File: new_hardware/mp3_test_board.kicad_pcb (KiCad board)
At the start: 2 copper layers, 110 x 56 mm, 126 parts, among them J1 PJ-322, J3 TF01-A, P1 TYPE-C 16PIN 2MD(073), P2 WF24LTYAJDNN0#, SW1 K2-1156SP-F5SW-05, SW2 K2-1156SP-F5SW-05, SW3 K2-1156SP-F5SW-05, SW4 K2-1156SP-F5SW-05, SW5 K2-1156SP-F5SW-05, SW6 K2-1156SP-F5SW-05, SW7 GT-TC054A-H035-L1, SW8 GT-TC054A-H035-L1, U1 PCM1795, U14 OPA1656, U15 OPA1656, U2 F133, U3 SGM6603-ADJYN6G, U4 SGM6603-ADJYN6G, U5 SGM3204, U6 LM4562, U7 LM4562, U8 USBLC6-2SC6, U9 MX25L25645GM2I-08G, Y1 12.88727

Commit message: some changes
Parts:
- added D3: PESD3V3L1BA, rlib_passive:D_SOD-323F, F.Cu at (137.2, 96.5)
- added R1: 4.7k, rlib_passive:R_0603_1608Metric, F.Cu at (121.9, 38.1)
- added R14: 10k, rlib_passive:R_0603_1608Metric, F.Cu at (125.9, 38.1)
- added R2: 4.7k, rlib_passive:R_0603_1608Metric, F.Cu at (125.9, 40.6)
- added R4: 1k, rlib_passive:R_0603_1608Metric, F.Cu at (121.9, 40.6)
- added R48: 10k, rlib_passive:R_0603_1608Metric, F.Cu at (96.2, 43.1)
- added R49: 220, rlib_passive:R_0603_1608Metric, F.Cu at (104.2, 43.1)
- added R5: R, rlib_passive:R_0603_1608Metric, F.Cu at (129.9, 38.1)
- added R50: 10k, rlib_passive:R_0603_1608Metric, F.Cu at (100.2, 40.6)
- added R51: 820, rlib_passive:R_0603_1608Metric, F.Cu at (100.2, 48.1)
- added R52: 820, rlib_passive:R_0603_1608Metric, F.Cu at (96.2, 45.6)
- added R53: 820, rlib_passive:R_0603_1608Metric, F.Cu at (96.2, 40.6)
- added R54: 820, rlib_passive:R_0603_1608Metric, F.Cu at (100.2, 43.1)
- added R55: 220, rlib_passive:R_0603_1608Metric, F.Cu at (104.2, 40.6)
- added R56: 220, rlib_passive:R_0603_1608Metric, F.Cu at (112.3, 38.1)
- added R57: 220, rlib_passive:R_0603_1608Metric, F.Cu at (96.2, 38.1)
- added R58: 200, rlib_passive:R_0603_1608Metric, F.Cu at (96.2, 48.1)
- added R59: 200, rlib_passive:R_0603_1608Metric, F.Cu at (108.3, 40.6)
- added R6: R, rlib_passive:R_0603_1608Metric, F.Cu at (129.9, 40.6)
- added R60: 200, rlib_passive:R_0603_1608Metric, F.Cu at (100.2, 45.6)
- added R61: 200, rlib_passive:R_0603_1608Metric, F.Cu at (104.2, 45.6)
- added R62: 180, rlib_passive:R_0603_1608Metric, F.Cu at (104.2, 38.1)
- added R63: 180, rlib_passive:R_0603_1608Metric, F.Cu at (100.2, 38.1)
- added R64: 180, rlib_passive:R_0603_1608Metric, F.Cu at (112.3, 40.6)
- added R65: 180, rlib_passive:R_0603_1608Metric, F.Cu at (108.3, 38.1)
- added R66: 50, rlib_passive:R_0603_1608Metric, F.Cu at (108.3, 43.1)
- added R67: 50, rlib_passive:R_0603_1608Metric, F.Cu at (104.2, 48.1)
- L1, L2: value 4.7u -> 1u
- P1: value TYPE-C 16PIN 2MD(073) -> USB-TYPE-C-018
- R38: value 100 -> 5.1
- moved P1 13.6 mm to (181.0, 99.3)
- moved J1 6.60 mm to (186.8, 72.3)
- moved SW2 4.06 mm to (162.1, 72.2)
- moved SW3 3.83 mm to (162.3, 86.7)
- moved U1 3.59 mm to (162.6, 99.1), turned to 0 degrees
- moved SW6 3.33 mm to (162.8, 101.4)
- moved P2 2.78 mm to (147.7, 108.0)
- moved U2 2.54 mm to (96.5, 86.4)
- moved SW4 2.23 mm to (173.1, 86.9)
- moved SW5 1.19 mm to (153.8, 86.7)
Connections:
- C35 pad 2: Net-(U2-Pad23) -> Net-(C35-Pad2)
- P2 pad 30: Net-(P2-Pad30) -> /SOC/LCD_EN
- R11 pad 1: Net-(P2-Pad30) -> /SOC/LCD_EN
- U2 pad 23: Net-(U2-Pad23) -> Net-(C35-Pad2)
- U2 pad 4: unconnected-(U2-Pad4) -> /SOC/LCD_EN
- U2 pad 53: /NewDAC/I2C_SCL -> /SOC/LCD_CS
- U2 pad 54: /NewDAC/I2C_SDIN -> /SOC/LCD_RD
- U2 pad 75: unconnected-(U2-Pad75) -> /SOC/LCD_WR
- U2 pad 76: unconnected-(U2-Pad76) -> /SOC/LCD_RS
- Y1 pad 1: Net-(U2-Pad23) -> Net-(C35-Pad2)
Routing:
- net /SOC/LCD_D5: track 0.00 -> 16.8 mm
- net GND: track 0.00 -> 0.81 mm

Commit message: xxxx
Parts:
- removed C104, C105, C108, C109, C80, C81, C84, C85, C86, C87, C88, C89, C90, C91: 10u, rlib_passive:T491A106K010AT
- removed C106, C107, C110, C111, C82, C83, C92, C93: 0.1u, rlib_passive:C_0603_1608Metric
- removed the D1 at (63.0, 51.8)
- removed the D1 at (86.4, 129.5)
- removed J3: TF01-A, rlib_connectors:TF-01A
- removed L9: L, rlib_passive:INDC2520X120N
- removed R51, R52, R53, R54: 820, rlib_passive:R_0603_1608Metric
- removed R55, R56, R57: 220, rlib_passive:R_0603_1608Metric
- removed R58, R59, R60, R61: 200, rlib_passive:R_0603_1608Metric
- removed R62, R63, R64, R65: 180, rlib_passive:R_0603_1608Metric
- removed R66, R67: 50, rlib_passive:R_0603_1608Metric
- removed U14, U15: OPA1656, rlib_ic:SOIC-8_3.9x4.9mm_P1.27mm
- removed the U4 at (94.2, 128.7)
- removed the U4 at (66.0, 121.9)
- removed the U5 at (12.7, 9.97)
- removed the U5 at (83.6, 135.8)
- added C1: 100n, rlib_passive:C_0603_1608Metric, F.Cu at (177.3, 118.3)
- added C16: 100n, rlib_passive:C_0603_1608Metric, B.Cu at (82.3, 61.1)
- added C2: 100n, rlib_passive:C_0603_1608Metric, F.Cu at (185.3, 116.6)
- added C3: 100n, rlib_passive:C_0603_1608Metric, B.Cu at (100.2, 63.3)
- added C37: 10u, rlib_passive:T491A106K010AT, B.Cu at (142.1, 73.1)
- added C38: 10u, rlib_passive:T491A106K010AT, B.Cu at (142.0, 67.5)
- added C39: 10u, rlib_passive:T491A106K010AT, B.Cu at (229.1, 125.3)
- added C4: 10u, rlib_passive:C_0603_1608Metric, B.Cu at (101.6, 64.7)
- added C40: 10u, rlib_passive:T491A106K010AT, B.Cu at (224.4, 125.3)
- added C41: 2.2n, rlib_passive:C_0603_1608Metric, B.Cu at (132.4, 87.9)
- added C42: 2.2n, rlib_passive:C_0603_1608Metric, F.Cu at (215.0, 139.9)
- added C43: 2.2n, rlib_passive:C_0603_1608Metric, F.Cu at (207.0, 139.9)
- added C44: 2.2n, rlib_passive:C_0603_1608Metric, B.Cu at (132.1, 79.4)
- added C45: 0.1u, rlib_passive:C_0603_1608Metric, B.Cu at (231.6, 134.0)
- added C46: 0.1u, rlib_passive:C_0603_1608Metric, B.Cu at (233.7, 139.1)
- added C48: 27n, rlib_passive:C_0603_1608Metric, F.Cu at (207.0, 137.4)
- added C49: 8n2, rlib_passive:C_0603_1608Metric, F.Cu at (207.0, 142.4)
- added C5: 18p, rlib_passive:C_0603_1608Metric, B.Cu at (79.9, 88.4)
- added C50: 8n2, rlib_passive:C_0603_1608Metric, F.Cu at (211.0, 142.4)
- added C51: 8n2, rlib_passive:C_0603_1608Metric, F.Cu at (215.0, 137.4)
- added C52: 8n2, rlib_passive:C_0603_1608Metric, F.Cu at (215.0, 142.4)
- added C53: 10u, rlib_passive:T491A106K010AT, B.Cu at (244.4, 139.8)
- added C54: 10u, rlib_passive:T491A106K010AT, B.Cu at (252.8, 152.9)
- added C55: 0.1u, rlib_passive:C_0603_1608Metric, B.Cu at (229.7, 136.5)
- added C56: 0.1u, rlib_passive:C_0603_1608Metric, B.Cu at (246.9, 148.0)
- added C57: 10u, rlib_passive:T491A106K010AT, B.Cu at (239.7, 137.5)
- added C58: 10u, rlib_passive:T491A106K010AT, B.Cu at (233.8, 125.3)
- added C59: 0.1u, rlib_passive:C_0603_1608Metric, B.Cu at (234.2, 141.6)
- added C61: 1u, rlib_passive:C_0603_1608Metric, B.Cu at (147.1, 54.5)
- added C62: 10u, rlib_passive:C_0603_1608Metric, B.Cu at (147.2, 49.6)
- added C63: 1u, rlib_passive:C_0603_1608Metric, B.Cu at (154.5, 44.8)
- added C64: 22u, rlib_passive:C_0603_1608Metric, B.Cu at (157.4, 57.0)
- added C65: 22u, rlib_passive:C_0603_1608Metric, B.Cu at (151.3, 57.1)
- added C68: 10u, rlib_passive:C_0603_1608Metric, B.Cu at (159.8, 49.6)
- added C69: 10u, rlib_passive:C_0603_1608Metric, B.Cu at (173.5, 62.4)
- added C72: 10u, rlib_passive:C_0603_1608Metric, B.Cu at (157.4, 68.2)
- added C73: 10u, rlib_passive:C_0603_1608Metric, B.Cu at (170.0, 68.7)
- added C74: 10u, rlib_passive:C_0603_1608Metric, B.Cu at (165.5, 73.5)
- added C75: 10u, rlib_passive:C_0603_1608Metric, B.Cu at (170.0, 71.2)
- added D1: PESD3V3L1BA, rlib_passive:D_SOD-323F, B.Cu at (105.3, 89.7)
- added H1: MountingHole, MountingHole:MountingHole_2.2mm_M2_DIN965_Pad, F.Cu at (79.9, 95.7)
- added H2: MountingHole, MountingHole:MountingHole_2.2mm_M2_DIN965_Pad, F.Cu at (79.9, 46.7)
- added H3: MountingHole, MountingHole:MountingHole_2.2mm_M2_DIN965_Pad, F.Cu at (172.9, 95.7)
- added H4: MountingHole, MountingHole:MountingHole_2.2mm_M2_DIN965_Pad, F.Cu at (172.9, 46.7)
- added J2: PJ-322, rlib_connectors:PJ-322, B.Cu at (175.8, 87.1)
- added L6: L, rlib_passive:INDC2520X120N, B.Cu at (165.6, 68.3)
- added Q1: 2N7002K, rlib_passive:SOT-23, F.Cu at (169.2, 110.6)
- added R15: 10k, rlib_passive:R_0603_1608Metric, B.Cu at (115.0, 45.6)
- added R16: 10k, rlib_passive:R_0603_1608Metric, B.Cu at (117.4, 45.5)
- added R17: 10k, rlib_passive:R_0603_1608Metric, F.Cu at (177.9, 112.8)
- added R18: 10k, rlib_passive:R_0603_1608Metric, B.Cu at (120.4, 45.5)
- added R19: 27, rlib_passive:R_0603_1608Metric, F.Cu at (180.8, 121.6)
- added R20: 27, rlib_passive:R_0603_1608Metric, F.Cu at (181.9, 114.1)
- added R21: 10k, rlib_passive:R_0603_1608Metric, F.Cu at (186.0, 114.1)
- added R22: 10k, rlib_passive:R_0603_1608Metric, F.Cu at (184.8, 121.6)
- added R23: 10k, rlib_passive:R_0603_1608Metric, B.Cu at (126.8, 74.4)
- added R24: 10k, rlib_passive:R_0603_1608Metric, B.Cu at (137.2, 62.6)
- added R25: 820, rlib_passive:R_0603_1608Metric, B.Cu at (136.1, 87.8)
- added R26: 820, rlib_passive:R_0603_1608Metric, B.Cu at (242.9, 145.5)
- added R27: 820, rlib_passive:R_0603_1608Metric, B.Cu at (229.7, 139.0)
- added R28: 820, rlib_passive:R_0603_1608Metric, B.Cu at (135.7, 79.2)
- added R41: 50, rlib_passive:R_0603_1608Metric, B.Cu at (218.4, 124.4)
- added R42: 50, rlib_passive:R_0603_1608Metric, B.Cu at (223.2, 127.7)
- added R45: 4.7k, rlib_passive:R_0603_1608Metric, B.Cu at (147.2, 46.1)
- added R46: 10k, rlib_passive:R_0603_1608Metric, B.Cu at (132.6, 141.2)
- added R47: R, rlib_passive:R_0603_1608Metric, B.Cu at (170.0, 66.6)
- added TP1: TestPoint, TestPoint:TestPoint_Pad_D1.0mm, F.Cu at (171.4, 137.3)
- added TP10: TestPoint, TestPoint:TestPoint_Pad_D1.0mm, F.Cu at (197.8, 106.5)
- added TP11: TestPoint, TestPoint:TestPoint_Pad_D1.0mm, F.Cu at (168.3, 140.4)
- added TP12: TestPoint, TestPoint:TestPoint_Pad_D1.0mm, F.Cu at (188.8, 119.4)
- added TP13: TestPoint, TestPoint:TestPoint_Pad_D1.0mm, B.Cu at (239.3, 148.2)
- added TP14: TestPoint, TestPoint:TestPoint_Pad_D1.0mm, B.Cu at (223.8, 133.0)
- added TP15: TestPoint, TestPoint:TestPoint_Pad_D1.0mm, B.Cu at (117.7, 129.1)
- added TP16: TestPoint, TestPoint:TestPoint_Pad_D1.0mm, B.Cu at (161.3, 55.4)
- added TP17: TestPoint, TestPoint:TestPoint_Pad_D1.0mm, B.Cu at (161.2, 52.7)
- added TP19: TestPoint, TestPoint:TestPoint_Pad_D1.0mm, B.Cu at (133.1, 144.0)
- added TP2: TestPoint, TestPoint:TestPoint_Pad_D1.0mm, F.Cu at (206.5, 100.4)
- added TP20: TestPoint, TestPoint:TestPoint_Pad_D1.0mm, B.Cu at (173.8, 70.4)
- added TP3: TestPoint, TestPoint:TestPoint_Pad_D1.0mm, F.Cu at (193.7, 111.5)
- added TP4: TestPoint, TestPoint:TestPoint_Pad_D1.0mm, F.Cu at (197.8, 109.5)
- added TP5: TestPoint, TestPoint:TestPoint_Pad_D1.0mm, F.Cu at (168.3, 137.3)
- added TP6: TestPoint, TestPoint:TestPoint_Pad_D1.0mm, F.Cu at (193.5, 114.6)
- added TP7: TestPoint, TestPoint:TestPoint_Pad_D1.0mm, F.Cu at (216.8, 92.2)
- added TP8: TestPoint, TestPoint:TestPoint_Pad_D1.0mm, F.Cu at (200.8, 106.5)
- added TP9: TestPoint, TestPoint:TestPoint_Pad_D1.0mm, F.Cu at (184.4, 124.4)
- added U10: SGM6603-ADJYN6G, rlib_power:SOT-23-6, B.Cu at (170.2, 62.9)
- added U11: SGM3204, rlib_power:SOT-23-6, B.Cu at (161.2, 68.2)
- added U4: PCM1795, rlib_ic:SSOP-28_5.3x10.2mm_P0.65mm, B.Cu at (134.0, 70.7)
- added U5: LM4562, rlib_ic:SOIC-8_3.9x4.9mm_P1.27mm, B.Cu at (134.1, 83.6)
- C10, C11, C12, C13, C14: value 10u -> 100n; footprint rlib_passive:T491A106K010AT -> rlib_passive:C_0603_1608Metric; moved to B.Cu
- C15, C17, C19, C22, C23, C28, D10, D12, D3, D9, F2, R14, Y1: moved to B.Cu
- C18, C20: value 10u -> 100n; moved to B.Cu
- C21: value 2.2u -> 100n; moved to B.Cu
- C29, C30, C31, C36: value 100n -> 10u; footprint rlib_passive:C_0603_1608Metric -> rlib_passive:T491A106K010AT; moved to B.Cu
- C32, C33: footprint rlib_passive:C_0603_1608Metric -> rlib_passive:R_0603_1608Metric; moved to B.Cu
- C34, C35, C60: value 100n -> 0.1u; moved to B.Cu
- C47: value 100n -> 27n
- C6: value 10u -> 18p; footprint rlib_passive:T491A106K010AT -> rlib_passive:C_0603_1608Metric; moved to B.Cu
- C66, C67, C70: value 100n -> 10u; moved to B.Cu
- C7: value 10u -> 100n; footprint rlib_passive:T491A106K010AT -> rlib_passive:C_0603_1608Metric
- C71: value 100n -> 3.3u; moved to B.Cu
- C8: footprint rlib_passive:T491A106K010AT -> rlib_passive:C_0603_1608Metric; moved to B.Cu
- C9: value 10u -> 2.2u; footprint rlib_passive:T491A106K010AT -> rlib_passive:C_0603_1608Metric; moved to B.Cu
- D11: value PESD3V3L1BA -> HCTL HC-1.25-3PWT; footprint rlib_passive:D_SOD-323F -> rlib_connectors:CONN-SMD_HC-1.25-3PWT; moved to B.Cu
- J1: value PJ-322 -> TF01-A; footprint rlib_connectors:PJ-322 -> rlib_connectors:TF-01A
- L1: value 1u -> L; footprint rlib_passive:IND_LQH32PN4R7NN0L -> rlib_passive:INDC2520X120N
- L2: footprint rlib_passive:IND_LQH32PN4R7NN0L -> rlib_passive:INDC2016X100N; moved to B.Cu
- L3: value 4.7u -> 1u; footprint rlib_passive:IND_LQH32PN4R7NN0L -> rlib_passive:INDC2016X100N
- L4: value 2.2u -> 4.7u; moved to B.Cu
- L5: value 2.2u -> L; footprint rlib_passive:IND_LQH32PN4R7NN0L -> rlib_passive:INDC2520X120N; moved to B.Cu
- P1: value USB-TYPE-C-018 -> WF24LTYAJDNN0#; footprint rlib_connectors:HRO-TYPE-C-31-M-12 -> rlib_lcd:WF24LTYAJDNN0; moved to F.Cu
- P2: value WF24LTYAJDNN0# -> USB-TYPE-C-018; footprint rlib_lcd:WF24LTYAJDNN0 -> rlib_connectors:HRO-TYPE-C-31-M-12; moved to B.Cu
- R1: value 4.7k -> 5.1
- R2: value 4.7k -> 10k
- R29, R30, R31, R32: value 10k -> 220; moved to B.Cu
- R33, R34, R35, R36: value 10k -> 200; moved to B.Cu
- R37, R39: value 10k -> 180; moved to B.Cu
- R38: value 5.1 -> 180; moved to B.Cu
- R4: value 1k -> 100
- R40: value 100 -> 180; moved to B.Cu
- R43: value 27 -> 4.7k; moved to B.Cu
- R44: value 27 -> 10k; moved to B.Cu
- R48: value 10k -> R; moved to B.Cu
- R49: value 220 -> 0; moved to B.Cu
- R5: value R -> 10k; moved to B.Cu
- R50: value 10k -> 0; moved to B.Cu
- R6: value R -> 50
- R7: value 50 -> 10k
- SW6: value K2-1156SP-F5SW-05 -> GT-TC054A-H035-L1; footprint rlib_buttons:K2-1156SP-F5SW-05 -> rlib_buttons:GT-TC054A-H035-L1
- U1: value PCM1795 -> F133; footprint rlib_ic:SSOP-28_5.3x10.2mm_P0.65mm -> rlib_ic:LQFP-128_14x14mm_P0.4mm
- U2: value F133 -> USBLC6-2SC6; footprint rlib_ic:LQFP-128_14x14mm_P0.4mm -> Package_TO_SOT_SMD:SOT-23-6; moved to F.Cu
- U3: value SGM6603-ADJYN6G -> MX25L25645GM2I-08G; footprint rlib_power:SOT-23-6 -> rlib_ic:SOIC-8_5.23x5.23mm_P1.27mm; moved to B.Cu
- U7: value LM4562 -> OPA1656
- U8: value USBLC6-2SC6 -> OPA1656; footprint Package_TO_SOT_SMD:SOT-23-6 -> rlib_ic:SOIC-8_3.9x4.9mm_P1.27mm; moved to B.Cu
- U9: value MX25L25645GM2I-08G -> AXP2101; footprint rlib_ic:SOIC-8_5.23x5.23mm_P1.27mm -> rlib_power:QFN-40_L5.0-W5.0-P0.40-TL-EP3.4; moved to B.Cu
- moved C35 203.9 mm to (242.9, 148.0), turned to 180 degrees
- moved L1 174.2 mm to (174.9, 106.8)
- moved L4 147.3 mm to (165.6, 62.7), turned to 90 degrees
- moved R13 146.0 mm to (190.2, 111.2)
- moved R9 145.8 mm to (186.2, 111.6)
- moved C26 145.6 mm to (189.3, 116.6)
- moved C27 145.6 mm to (185.3, 119.1)
- moved L2 144.0 mm to (157.3, 54.5)
- moved C25 137.0 mm to (176.8, 130.8)
- moved R7 136.9 mm to (168.8, 132.1)
- moved C24 132.8 mm to (168.8, 127.0)
- moved F2 132.0 mm to (146.2, 57.2), turned to 180 degrees
- moved R10 127.2 mm to (168.8, 117.0)
- moved C33 126.2 mm to (143.5, 65.4)
- moved R29 123.4 mm to (251.6, 157.8), turned to 180 degrees
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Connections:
- C10 pad 1: +2V5 -> +3V3
- C12 pad 1: +1V1 -> +1V8
- C13 pad 1: VCC -> +1V8
- C14 pad 1: +5VA -> +1V8
- C17 pad 1: +1V8 -> +3V3
- C19 pad 1: GND -> +3V3
- C19 pad 2: Net-(C19-Pad2) -> GND
- C20 pad 1: +3V3 -> Net-(C20-Pad1)
- C21 pad 1: +1V8 -> +3V3
- C22 pad 1: +3V3 -> +1V8
- C24 pad 1: +1V8 -> VBUS
- C25 pad 1: +1V8 -> Net-(C25-Pad1)
- C26 pad 1: +1V8 -> GND
- C26 pad 2: GND -> +3V3
- C29 pad 1: +3V3 -> GNDA
- C29 pad 2: GND -> +5VA
- C30 pad 1: +3V3 -> GNDA
- C30 pad 2: GND -> -5VA
- C31 pad 1: +3V3 -> +5VA
- C31 pad 2: GND -> Net-(C31-Pad2)
- C32 pad 1: +3V3 -> +5VA
- C32 pad 2: GND -> GNDA
- C33 pad 1: +1V8 -> +5VA
- C33 pad 2: GND -> GNDA
- C34 pad 1: +1V8 -> GNDA
- C34 pad 2: GND -> +5VA
- C35 pad 1: GND -> -5VA
- C35 pad 2: Net-(C35-Pad2) -> GNDA
- C36 pad 1: +1V8 -> +5VA
- C36 pad 2: GND -> GNDA
- C47 pad 1: GND -> Net-(C47-Pad1)
- C47 pad 2: +3V3 -> Net-(C47-Pad2)
- C6 pad 1: VCC -> GND
- C6 pad 2: GND -> Net-(C6-Pad2)
- C60 pad 1: Net-(C60-Pad1) -> -5VA
- C60 pad 2: GND -> GNDA
- C66 pad 1: +3V3 -> Net-(C66-Pad1)
- C67 pad 1: +3V3 -> VCC
- C7 pad 1: VCC -> +1V8
- C70 pad 1: VBUS -> +5VA
- C70 pad 2: GND -> GNDA
- C71 pad 2: GND -> Net-(C71-Pad2)
- C8 pad 1: VCC -> +3V3
- C9 pad 1: VCC -> +1V8
- D10 pad 1: GND -> GNDA
- D10 pad 2: /SOC/SDC_D2 -> Net-(D10-Pad2)
- D11 pad 1: GNDA -> Net-(D11-Pad1)
- D11 pad 2: Net-(D11-Pad2) -> unconnected-(D11-Pad2)
- D12 pad 1: GNDA -> Net-(D12-Pad1)
- D12 pad 2: Net-(D12-Pad2) -> GND
- D2 pad 1: Net-(D2-Pad1) -> GND
- D2 pad 2: GND -> /SOC/SDC_D1
- D3 pad 2: /SOC/SDC_PLUG -> /SOC/SDC_D0
- D4 pad 2: Net-(C60-Pad1) -> /SOC/SDC_CLK
- D5 pad 2: /SOC/SDC_D1 -> /SOC/SDC_CMD
- D6 pad 2: /SOC/SDC_D0 -> /SOC/SDC_D3
- D7 pad 2: /SOC/SDC_CLK -> /SOC/SDC_D2
- D8 pad 2: /SOC/SDC_CMD -> /SOC/SDC_PLUG
- D9 pad 1: GND -> GNDA
- D9 pad 2: /SOC/SDC_D3 -> Net-(D9-Pad2)
- F1 pad 1: Net-(D1-Pad1) -> Net-(C25-Pad1)
- F1 pad 2: Net-(C1-Pad1) -> Net-(F1-Pad2)
- F2 pad 1: Net-(C71-Pad1) -> Net-(D11-Pad1)
- F2 pad 2: Net-(F2-Pad2) -> Net-(C61-Pad1)
- J1 pad 1: GNDA -> /SOC/SDC_D2
- J1 pad 2: unconnected-(J1-Pad2) -> /SOC/SDC_D3
- J1 pad 3: Net-(D12-Pad2) -> /SOC/SDC_CMD
- J1 pad 4: Net-(D11-Pad2) -> +3V3
- L1 pad 1: Net-(L1-Pad1) -> VBUS
- L1 pad 2: +3V3 -> Net-(C25-Pad1)
- L3 pad 1: VCC -> Net-(L3-Pad1)
- L3 pad 2: Net-(L3-Pad2) -> +3V3
- L4 pad 1: Net-(C12-Pad1) -> VCC
- L4 pad 2: -5VA -> Net-(L4-Pad2)
- L5 pad 1: Net-(C13-Pad1) -> Net-(C72-Pad1)
- L5 pad 2: +5VA -> -5VA
- R1 pad 1: /NewDAC/I2C_SCL -> Net-(P1-Pad38)
- R1 pad 2: +3V3 -> Net-(Q1-Pad3)
- R10 pad 1: /SOC/FLASH_SPI_CS -> Net-(R10-Pad1)
- R10 pad 2: +3V3 -> Net-(R10-Pad2)
- R11 pad 1: /SOC/LCD_EN -> Net-(R10-Pad2)
- R11 pad 2: +3V3 -> Net-(R11-Pad2)
- R12 pad 1: /SOC/SDC_PLUG -> Net-(R11-Pad2)
- R12 pad 2: +3V3 -> Net-(R12-Pad2)
- R13 pad 1: /SOC/FLASH_SPI_MISO -> Net-(R12-Pad2)
- R13 pad 2: +3V3 -> Net-(C20-Pad1)
- R14 pad 1: GND -> +3V3
- R14 pad 2: /Power/AUDIO_PWR_EN -> /SOC/SDC_D2
- R2 pad 1: /NewDAC/I2C_SDIN -> Net-(Q1-Pad1)
- R2 pad 2: +3V3 -> GND
- R29 pad 1: Net-(R29-Pad1) -> Net-(C42-Pad2)
- R29 pad 2: Net-(R29-Pad2) -> Net-(C48-Pad2)
- R3 pad 1: +3V3 -> /SOC/LCD_EN
- R3 pad 2: /SOC/KEYS -> +3V3
- R30 pad 1: Net-(R29-Pad2) -> Net-(C43-Pad2)
- R30 pad 2: Net-(R30-Pad2) -> Net-(C48-Pad1)
- R31 pad 1: Net-(R30-Pad2) -> Net-(C41-Pad2)
- R31 pad 2: Net-(R31-Pad2) -> Net-(C47-Pad2)
- R32 pad 1: Net-(R31-Pad2) -> Net-(C44-Pad2)
- R32 pad 2: Net-(R32-Pad2) -> Net-(C47-Pad1)
- R33 pad 1: Net-(R32-Pad2) -> Net-(C47-Pad2)
- R33 pad 2: Net-(C60-Pad1) -> Net-(C49-Pad2)
- R34 pad 1: +3V3 -> GNDA
- R34 pad 2: /SOC/SDC_D2 -> Net-(C47-Pad1)
- R35 pad 1: +3V3 -> Net-(C48-Pad2)
- R35 pad 2: /SOC/SDC_D3 -> Net-(C51-Pad2)
- R36 pad 1: +3V3 -> GNDA
- R36 pad 2: /SOC/SDC_D0 -> Net-(C48-Pad1)
- R37 pad 1: +3V3 -> Net-(C47-Pad2)
- R37 pad 2: /SOC/SDC_D1 -> Net-(C49-Pad1)
- R38 pad 1: Net-(P2-Pad38) -> Net-(C47-Pad1)
- R38 pad 2: Net-(Q1-Pad1) -> Net-(C50-Pad2)
- R39 pad 1: Net-(Q1-Pad3) -> Net-(C48-Pad2)
- R39 pad 2: GND -> Net-(C51-Pad1)
- R4 pad 1: GND -> Net-(Q1-Pad1)
- R4 pad 2: Net-(R4-Pad2) -> /SOC/LCD_PWM
- R40 pad 1: Net-(Q1-Pad3) -> Net-(C48-Pad1)
- R40 pad 2: /SOC/LCD_PWM -> Net-(C52-Pad2)
- R43 pad 1: /SOC/USB_DM -> /NewDAC/I2C_SCL
- R43 pad 2: Net-(R43-Pad2) -> +3V3
- R44 pad 1: /SOC/USB_DP -> GND
- R48 pad 1: +3V3 -> GNDA
- R48 pad 2: Net-(R48-Pad2) -> Net-(R47-Pad1)
- R49 pad 1: Net-(C94-Pad2) -> Net-(R49-Pad1)
- R49 pad 2: Net-(C98-Pad2) -> VCC
- R5 pad 1: Net-(R5-Pad1) -> +3V3
- R5 pad 2: Net-(C13-Pad1) -> /SOC/KEYS
- R50 pad 2: GNDA -> VCC
- R6 pad 1: GNDA -> Net-(JP1-Pad2)
- R6 pad 2: Net-(R5-Pad1) -> /SOC/FLASH_SPI_CS
- R7 pad 1: Net-(JP1-Pad2) -> /SOC/KEYS
- R7 pad 2: /SOC/FLASH_SPI_CS -> Net-(R7-Pad2)
- R8 pad 1: /SOC/KEYS -> /Power/RESET
- R8 pad 2: Net-(R29-Pad1) -> +3V3
- R9 pad 1: /Power/RESET -> Net-(R7-Pad2)
- R9 pad 2: +3V3 -> Net-(R10-Pad1)
- SW1 pad 1: GND -> /SOC/KEYS
- SW1 pad 2: GND -> /SOC/KEYS
- SW1 pad 3: Net-(U2-Pad23) -> GND
- SW1 pad 4: Net-(U2-Pad23) -> GND
- SW2 pad 1: /SOC/KEYS -> Net-(R7-Pad2)
- SW2 pad 2: /SOC/KEYS -> Net-(R7-Pad2)
- SW3 pad 1: Net-(R29-Pad1) -> Net-(R10-Pad1)
- SW3 pad 2: Net-(R29-Pad1) -> Net-(R10-Pad1)
- SW4 pad 1: Net-(R29-Pad2) -> Net-(R10-Pad2)
- SW4 pad 2: Net-(R29-Pad2) -> Net-(R10-Pad2)
- SW5 pad 1: Net-(R30-Pad2) -> Net-(R11-Pad2)
- SW5 pad 2: Net-(R30-Pad2) -> Net-(R11-Pad2)
- SW6 pad 1: Net-(R31-Pad2) -> Net-(R12-Pad2)
- SW6 pad 2: Net-(R31-Pad2) -> GND
- SW6 pad 3: GND -> (no net)
- SW6 pad 4: GND -> (no net)
- SW7 pad 1: Net-(R32-Pad2) -> Net-(C20-Pad1)
- SW8 pad 1: Net-(C60-Pad1) -> GND
- SW8 pad 2: GND -> Net-(D12-Pad1)
- U1 pad 1: unconnected-(U1-Pad1) -> /SOC/SDC_PLUG
- U1 pad 10: GND -> unconnected-(U1-Pad10)
- U1 pad 11: /NewDAC/I2C_SDIN -> unconnected-(U1-Pad11)
- U1 pad 12: /NewDAC/I2C_SCL -> unconnected-(U1-Pad12)
- U1 pad 14: GND -> /SOC/FLASH_SPI_HOLD
- U1 pad 15: +5VA -> /SOC/FLASH_SPI_WP
- U1 pad 16: GNDA -> /SOC/FLASH_SPI_CS
- U1 pad 17: Net-(C96-Pad1) -> /SOC/FLASH_SPI_MOSI
- U1 pad 18: Net-(C97-Pad1) -> /SOC/FLASH_SPI_CS
- U1 pad 19: GNDA -> /SOC/FLASH_SPI_CLK
- U1 pad 2: unconnected-(U1-Pad2) -> /SOC/LCD_EN
- U1 pad 20: Net-(R50-Pad1) -> +1V8
- U1 pad 21: Net-(C84-Pad2) -> unconnected-(U1-Pad21)
- U1 pad 22: Net-(C84-Pad2) -> Net-(C5-Pad2)
- U1 pad 23: +5VA -> Net-(C6-Pad2)
- U1 pad 24: GNDA -> unconnected-(U1-Pad24)
- U1 pad 25: Net-(C94-Pad1) -> unconnected-(U1-Pad25)
- U1 pad 26: Net-(C95-Pad1) -> +1V8
- U1 pad 27: GNDA -> /Power/RESET
- U1 pad 28: +5VA -> +1V8
- U1 pad 3: Net-(R48-Pad2) -> /NewDAC/I2C_SDIN
- U1 pad 4: /NewDAC/I2S_LRCK -> /NewDAC/I2C_SCL
- U1 pad 5: /NewDAC/I2S_DIN -> /SOC/LCD_PWM
- U1 pad 6: /NewDAC/I2S_BCLK -> /NewDAC/I2S_MCLK
- U1 pad 7: /NewDAC/I2S_MCLK -> unconnected-(U1-Pad7)
- U1 pad 8: GND -> unconnected-(U1-Pad8)
- U1 pad 9: +3V3 -> unconnected-(U1-Pad9)
- U2 pad 1: /SOC/SDC_PLUG -> Net-(R19-Pad2)
- U2 pad 2: unconnected-(U2-Pad2) -> GND
- U2 pad 3: unconnected-(U2-Pad3) -> Net-(R20-Pad2)
- U2 pad 4: /SOC/LCD_EN -> Net-(P2-PadA6)
- U2 pad 5: /SOC/LCD_PWM -> VBUS
- U2 pad 6: /NewDAC/I2S_MCLK -> Net-(P2-PadA7)
- U3 pad 1: Net-(L4-Pad2) -> /SOC/FLASH_SPI_CS
- U3 pad 2: GND -> /SOC/FLASH_SPI_CS
- U3 pad 3: VCC -> /SOC/FLASH_SPI_WP
- U3 pad 4: Net-(R10-Pad2) -> GND
- U3 pad 5: Net-(C17-Pad1) -> /SOC/FLASH_SPI_MOSI
- U3 pad 6: VCC -> /SOC/FLASH_SPI_CLK
- U6 pad 1: Net-(C94-Pad2) -> Net-(C42-Pad2)
- U6 pad 2: Net-(C94-Pad1) -> Net-(C42-Pad1)
- U6 pad 6: Net-(C95-Pad1) -> Net-(C43-Pad1)
- U6 pad 7: Net-(C95-Pad2) -> Net-(C43-Pad2)
- U7 pad 1: Net-(C96-Pad2) -> Net-(C49-Pad2)
- U7 pad 2: Net-(C96-Pad1) -> Net-(C50-Pad2)
- U7 pad 3: GNDA -> Net-(C49-Pad1)
- U7 pad 5: GNDA -> (no net)
- U7 pad 6: Net-(C97-Pad1) -> (no net)
- U7 pad 7: Net-(C97-Pad2) -> (no net)
- U8 pad 1: Net-(R43-Pad2) -> Net-(C51-Pad2)
- U8 pad 2: GND -> Net-(C52-Pad2)
- U8 pad 3: Net-(R44-Pad2) -> Net-(C51-Pad1)
- U8 pad 4: Net-(P1-PadA6) -> -5VA
- U8 pad 5: VBUS -> (no net)
- U8 pad 6: Net-(P1-PadA7) -> (no net)
- U9 pad 1: /SOC/FLASH_SPI_CS -> unconnected-(U9-Pad1)
- U9 pad 2: /SOC/FLASH_SPI_MISO -> Net-(C63-Pad2)
- U9 pad 3: /SOC/FLASH_SPI_WP -> GND
- U9 pad 4: GND -> unconnected-(U9-Pad4)
- U9 pad 5: /SOC/FLASH_SPI_MOSI -> unconnected-(U9-Pad5)
- U9 pad 6: /SOC/FLASH_SPI_CLK -> unconnected-(U9-Pad6)
- U9 pad 7: /SOC/FLASH_SPI_HOLD -> unconnected-(U9-Pad7)
- U9 pad 8: +3V3 -> unconnected-(U9-Pad8)
- Y1 pad 1: Net-(C35-Pad2) -> Net-(C6-Pad2)
- Y1 pad 3: Net-(C19-Pad2) -> Net-(C5-Pad2)
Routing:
- net /SOC/LCD_D5: track 16.8 -> 0.00 mm
- net GND: track 0.81 -> 0.00 mm
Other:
- board size 110 x 56 mm -> 100 x 56 mm

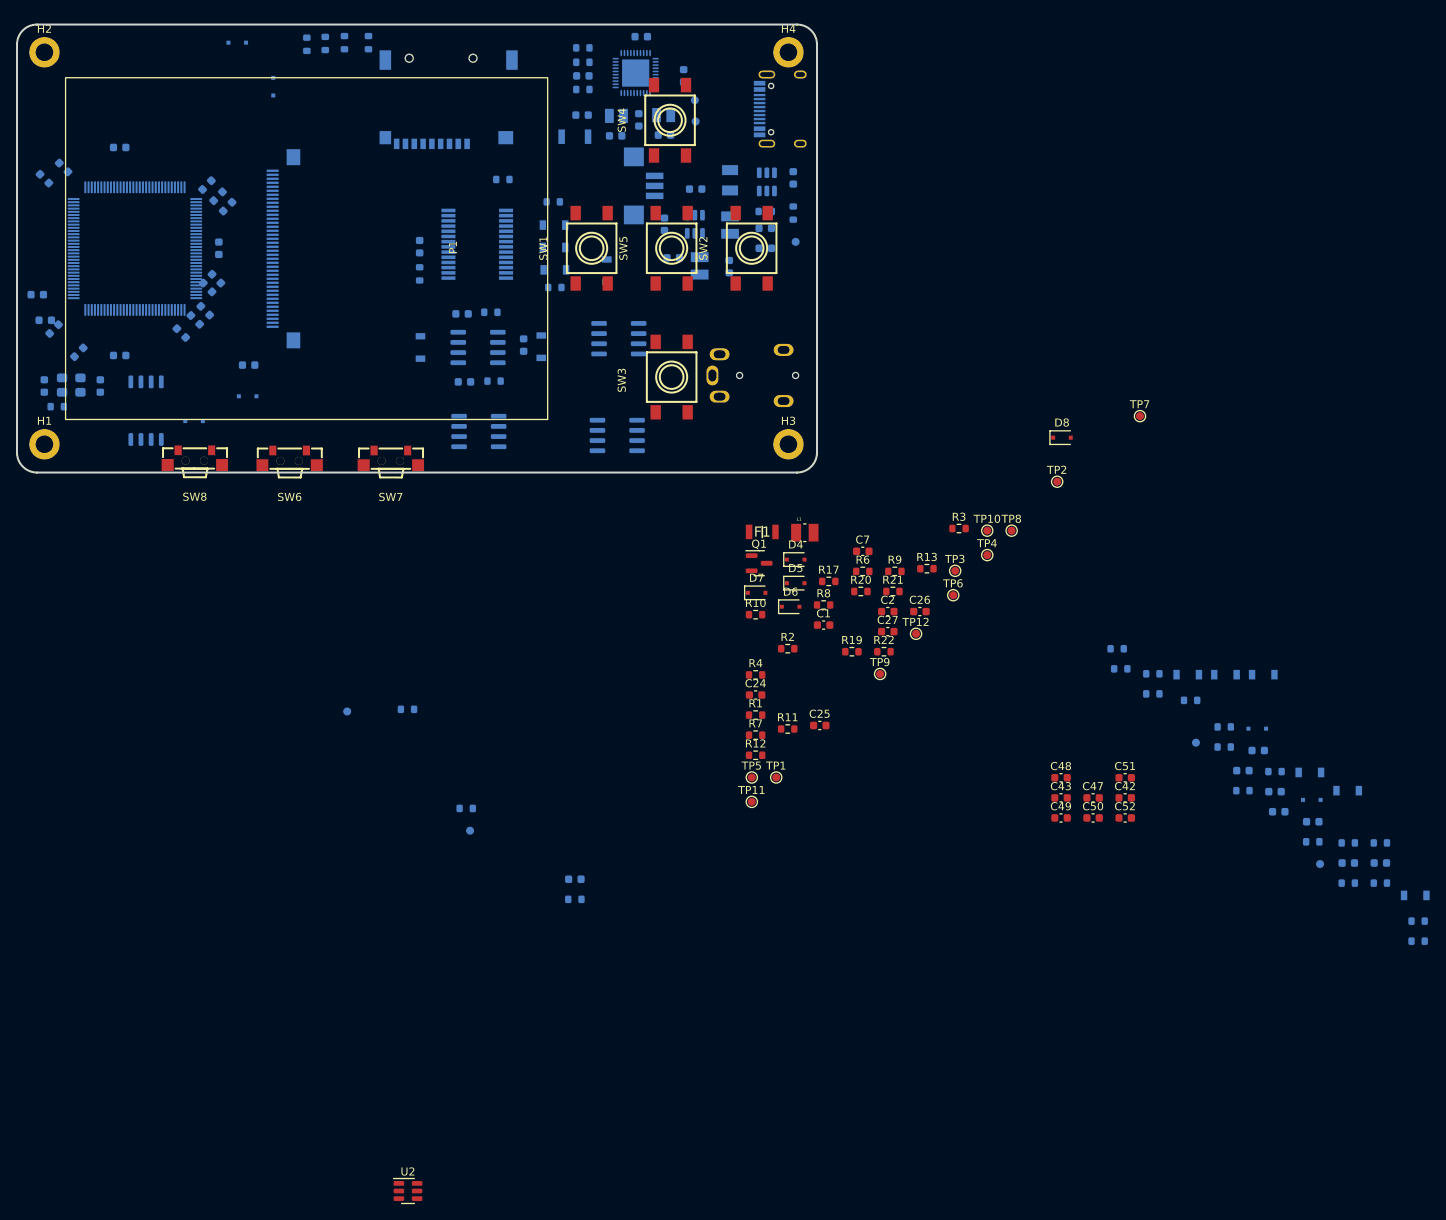
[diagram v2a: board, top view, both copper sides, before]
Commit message: changed lcd interface and layout is partly made
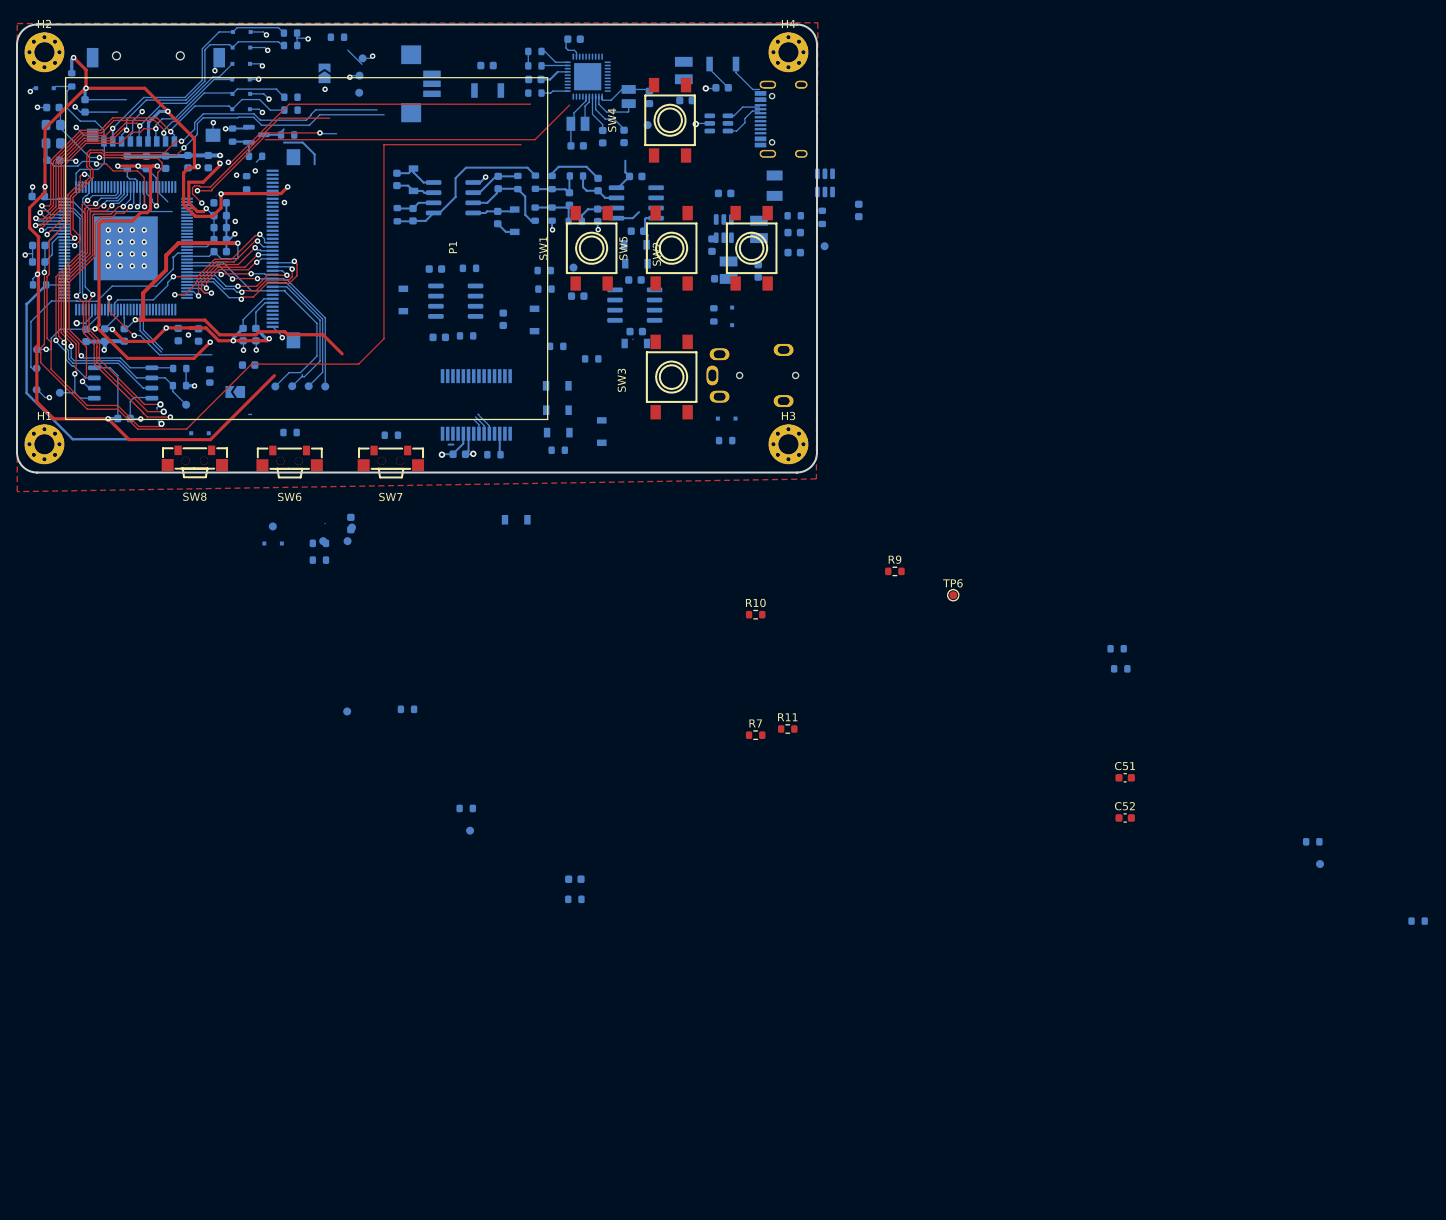
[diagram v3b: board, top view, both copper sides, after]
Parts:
- added JP1: Jumper_2_Open, Jumper:SolderJumper-2_P1.3mm_Open_TrianglePad1.0x1.5mm, B.Cu at (103.8, 89.2)
- added JP2: Jumper_2_Open, Jumper:SolderJumper-2_P1.3mm_Open_TrianglePad1.0x1.5mm, B.Cu at (114.9, 49.3)
- added TP18: TestPoint, TestPoint:TestPoint_Pad_D1.0mm, B.Cu at (118.3, 106.1)
- added TP21: TestPoint, TestPoint:TestPoint_Pad_D1.0mm, B.Cu at (117.8, 107.8)
- added TP22: TestPoint, TestPoint:TestPoint_Pad_D1.0mm, B.Cu at (108.5, 106.0)
- added TP23: TestPoint, TestPoint:TestPoint_Pad_D1.0mm, B.Cu at (114.7, 107.8)
- C1, C2, C24, C25, C26, C27, C42, C43, C47, C48, C49, C50, C7, D4, D5, D6, D7, D8, F1, L1, Q1, R1, R12, R13, R17, R19, R2, R20, R21, R22, R3, R4, R6, R8, TP1, TP10, TP11, TP12, TP2, TP3, TP4, TP5, TP7, TP8, TP9, U2: moved to B.Cu
- C12: value 100n -> 10u
- C13: value 100n -> 1u
- H1, H2, H3, H4: footprint MountingHole:MountingHole_2.2mm_M2_DIN965_Pad -> MountingHole:MountingHole_2.5mm_Pad_Via
- moved C35 146.4 mm to (124.0, 62.6), turned to -90 degrees
- moved U2 139.0 mm to (164.2, 55.6)
- moved TP7 138.0 mm to (78.9, 86.2), turned to 180 degrees
- moved R29 137.7 mm to (142.4, 74.0)
- moved D8 134.4 mm to (80.0, 51.2)
- moved R26 131.2 mm to (133.0, 73.7), turned to 0 degrees
- moved R37 130.6 mm to (146.4, 62.2), turned to 0 degrees
- moved R38 130.3 mm to (146.2, 67.8), turned to 0 degrees
- moved C56 126.6 mm to (153.8, 62.2), turned to 0 degrees
- moved R30 124.9 mm to (142.5, 76.3)
- moved R22 124.2 mm to (83.3, 50.1), turned to 90 degrees
- moved C54 121.8 mm to (140.5, 105.9)
- moved C27 120.0 mm to (85.0, 53.4), turned to -90 degrees
- moved C45 116.9 mm to (118.2, 105.6), turned to 90 degrees
- moved R32 115.8 mm to (141.2, 66.9), turned to 90 degrees
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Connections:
- C12 pad 1: +1V8 -> +1V8B
- C13 pad 1: +1V8 -> +1V8B
- C14 pad 1: +1V8 -> +1V8B
- C15 pad 1: +3V3 -> +0V9
- C16 pad 1: +3V3 -> +0V9
- C17 pad 1: +3V3 -> +0V9
- C18 pad 1: +1V8 -> +1V8A
- C19 pad 1: +3V3 -> +0V9
- C22 pad 1: +1V8 -> +1V8A
- C29 pad 1: GNDA -> +5VA
- C29 pad 2: +5VA -> GNDA
- C3 pad 1: +1V8 -> +1V8A
- C39 pad 1: GNDA -> +5VA
- C39 pad 2: +5VA -> GNDA
- C4 pad 1: +1V8 -> +1V8A
- C53 pad 1: GNDA -> +5VA
- C53 pad 2: +5VA -> GNDA
- C57 pad 1: GNDA -> +5VA
- C57 pad 2: +5VA -> GNDA
- C65 pad 1: +3V3 -> +0V9
- C7 pad 1: +1V8 -> +1V8A
- C9 pad 1: +1V8 -> +1V8B
- L3 pad 2: +3V3 -> +0V9
- P1 pad 14: /SOC/LCD_D0 -> /SOC/LCD_D3
- P1 pad 15: /SOC/LCD_D1 -> /SOC/LCD_D4
- P1 pad 16: /SOC/LCD_D2 -> /SOC/LCD_D5
- P1 pad 17: /SOC/LCD_D3 -> /SOC/LCD_D6
- P1 pad 18: /SOC/LCD_D4 -> /SOC/LCD_D7
- P1 pad 19: /SOC/LCD_D5 -> /SOC/LCD_D10
- P1 pad 20: /SOC/LCD_D6 -> /SOC/LCD_D11
- P1 pad 21: /SOC/LCD_D7 -> /SOC/LCD_D12
- P1 pad 22: /SOC/LCD_D8 -> unconnected-(P1-Pad22)
- P1 pad 23: /SOC/LCD_D9 -> GND
- P1 pad 24: /SOC/LCD_D10 -> GND
- P1 pad 25: /SOC/LCD_D11 -> GND
- P1 pad 26: /SOC/LCD_D12 -> GND
- P1 pad 27: /SOC/LCD_D13 -> GND
- P1 pad 28: /SOC/LCD_D14 -> GND
- P1 pad 29: /SOC/LCD_D15 -> GND
- P1 pad 30: /SOC/LCD_EN -> Net-(P1-Pad30)
- R21 pad 1: /SOC/FLASH_SPI_CS -> /SOC/FLASH_SPI_MISO
- R3 pad 1: /SOC/LCD_EN -> Net-(P1-Pad30)
- TP11 pad 1: /SOC/FLASH_SPI_CS -> /SOC/FLASH_SPI_MISO
- TP17 pad 1: +3V3 -> +0V9
- TP5 pad 1: +1V8 -> +1V8A
- TP7 pad 1: unconnected-(TP7-Pad1) -> +1V8B
- U1 pad 116: +3V3 -> +0V9
- U1 pad 117: +3V3 -> +0V9
- U1 pad 16: /SOC/FLASH_SPI_CS -> /SOC/FLASH_SPI_MISO
- U1 pad 20: +1V8 -> +1V8A
- U1 pad 26: +1V8 -> +1V8A
- U1 pad 28: +1V8 -> +1V8A
- U1 pad 30: +1V8 -> +1V8B
- U1 pad 31: unconnected-(U1-Pad31) -> /Power/IRQ
- U1 pad 48: +1V8 -> +1V8B
- U1 pad 49: +1V8 -> +1V8B
- U1 pad 50: +1V8 -> +1V8B
- U1 pad 51: +3V3 -> +0V9
- U1 pad 65: +1V8 -> +1V8A
- U1 pad 81: +3V3 -> +0V9
- U1 pad 89: +1V8 -> +1V8A
- U3 pad 2: /SOC/FLASH_SPI_CS -> /SOC/FLASH_SPI_MISO
- U9 pad 26: +3V3 -> +0V9
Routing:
- net +3V3: track 0.00 -> 296.9 mm, vias 0 -> 18
- net +0V9: track 0.00 -> 216.0 mm, vias 0 -> 4
- net GND: track 0.00 -> 90.0 mm, vias 0 -> 49
- net +1V8A: track 0.00 -> 71.2 mm, vias 0 -> 6
- net /SOC/USB_DP: track 0.00 -> 55.5 mm, vias 0 -> 2
- net /SOC/USB_DM: track 0.00 -> 53.6 mm, vias 0 -> 2
- net /SOC/SDC_D1: track 0.00 -> 52.3 mm, vias 0 -> 2
- net /SOC/SDC_D0: track 0.00 -> 51.9 mm, vias 0 -> 2
- net +1V8B: track 0.00 -> 49.3 mm, vias 0 -> 2
- net /NewDAC/I2S_MCLK: track 0.00 -> 48.4 mm, vias 0 -> 2
- net /SOC/SDC_D3: track 0.00 -> 46.8 mm, vias 0 -> 2
- net /SOC/SDC_D2: track 0.00 -> 46.1 mm, vias 0 -> 2
- net /SOC/FLASH_SPI_MISO: track 0.00 -> 44.1 mm, vias 0 -> 2
- net /Power/RESET: track 0.00 -> 42.2 mm
- net /SOC/SDC_CLK: track 0.00 -> 42.1 mm, vias 0 -> 2
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- added copper zone on F.Cu, net GND
- added copper zone on In2.Cu, net GND
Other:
- copper layers 2 -> 4
